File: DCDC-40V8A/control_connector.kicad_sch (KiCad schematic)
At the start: 2 parts, among them J5 Conn_01x08_MountingPin, J6 Conn_01x08_MountingPin

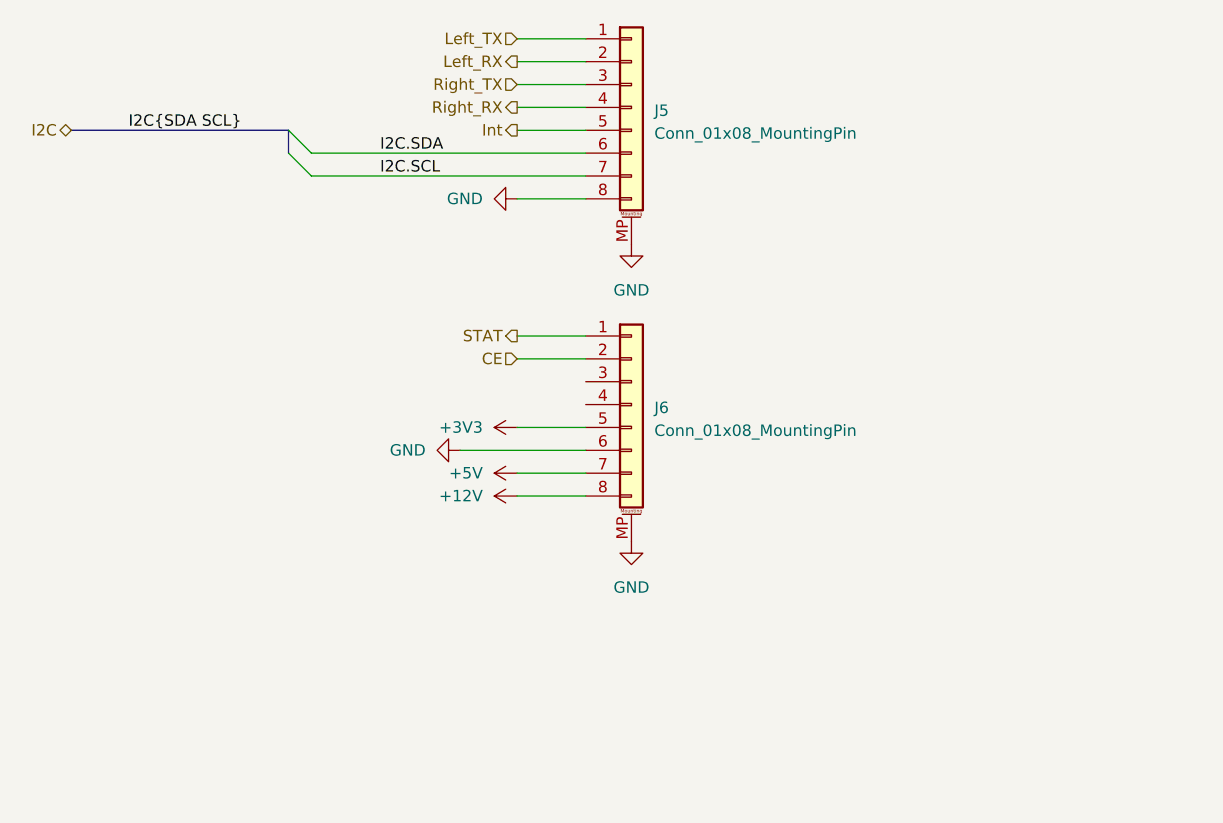
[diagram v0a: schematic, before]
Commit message: some DCDC schematics
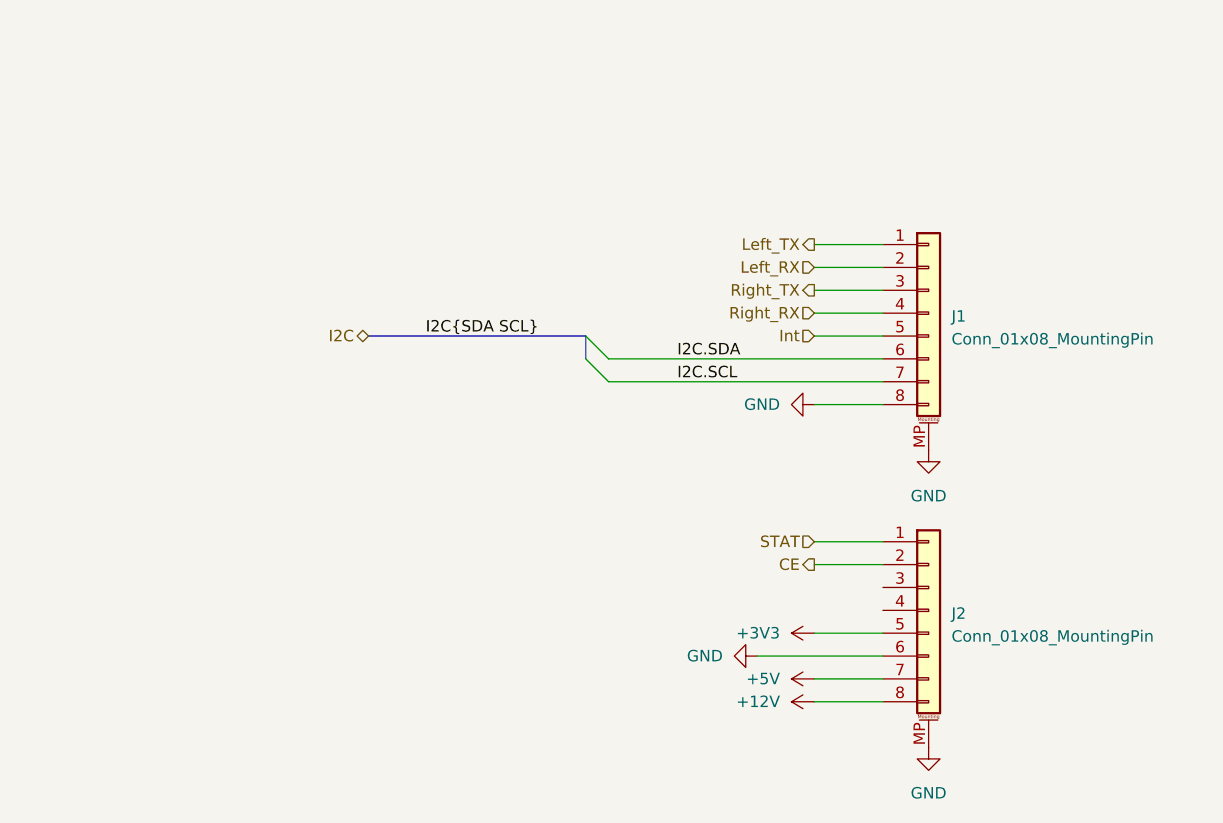
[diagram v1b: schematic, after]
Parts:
- removed J5, J6: Conn_01x08_MountingPin, Connector_JST:JST_SH_SM08B-SRSS-TB_1x08-1MP_P1.00mm_Horizontal, symbol Connector_Generic_MountingPin:Conn_01x08_MountingPin
- added J1, J2: Conn_01x08_MountingPin, Connector_JST:JST_SH_BM08B-SRSS-TB_1x08-1MP_P1.00mm_Vertical, symbol Connector_Generic_MountingPin:Conn_01x08_MountingPin
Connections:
- net +12V: now also J2.8 (Pin_8)
- net +3V3: now also J2.5 (Pin_5)
- net +5V: now also J2.7 (Pin_7)
- net CE: now also J2.2 (Pin_2)
- net GND: now also J1.8 (Pin_8), J1.MP (MountPin), J2.6 (Pin_6), J2.MP (MountPin)
- net I2C.SCL: now also J1.7 (Pin_7)
- net I2C.SDA: now also J1.6 (Pin_6)
- net Int: now also J1.5 (Pin_5)
- net Left_RX: now also J1.2 (Pin_2)
- net Left_TX: now also J1.1 (Pin_1)
- net Right_RX: now also J1.4 (Pin_4)
- net Right_TX: now also J1.3 (Pin_3)
- net STAT: now also J2.1 (Pin_1)

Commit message: wip
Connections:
- net +5V_USB: now reaches J2.3 (Pin_3)
- net +5V_USB: now also J2.4 (Pin_4)
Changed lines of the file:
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@@
 	(generator_version "9.0")
 	(paper "A4")
+	(junction
+		(at 137.16 97.79)
+		(diameter 0)
+		(color 0 0 0 0)
+	)
 	(bus_entry
 		(at 111.76 71.12)
@@
 	(wire
 		(pts
+			(xy 137.16 96.52) (xy 137.16 97.79)
+		)
+		(stroke
+			(width 0)
+			(type default)
+		)
+	)
+	(wire
+		(pts
 			(xy 137.16 63.5) (xy 144.78 63.5)
+		)
+		(stroke
+			(width 0)
+			(type default)
+		)
+	)
+	(wire
+		(pts
+			(xy 144.78 96.52) (xy 137.16 96.52)
+		)
+		(stroke
+			(width 0)
+			(type default)
+		)
+	)
+	(wire
+		(pts
+			(xy 137.16 99.06) (xy 144.78 99.06)
+		)
+		(stroke
+			(width 0)
+			(type default)
+		)
+	)
+	(wire
+		(pts
+			(xy 137.16 97.79) (xy 137.16 99.06)
 		)
 		(stroke
@@
 		)
 	)
+	(symbol
+		(lib_id "power:+5V")
+		(at 137.16 97.79 90)
+		(unit 1)
+		(exclude_from_sim no)
+		(in_bom yes)
+		(on_board yes)
+		(dnp no)
+		(fields_autoplaced yes)
+		(property "Reference" "#PWR054"
+			(at 140.97 97.79 0)
+			(effects
+				(font
+					(size 1.27 1.27)
+				)
+				(hide yes)
+			)
+		)
+		(property "Value" "+5V_USB"
+			(at 133.35 97.7899 90)
+			(effects
+				(font
+					(size 1.27 1.27)
+				)
+				(justify left)
+			)
+		)
+		(property "Footprint" ""
+			(at 137.16 97.79 0)
+			(effects
+				(font
+					(size 1.27 1.27)
+				)
+				(hide yes)
+			)
+		)
+		(property "Datasheet" ""
+			(at 137.16 97.79 0)
+			(effects
+				(font
+					(size 1.27 1.27)
+				)
+				(hide yes)
+			)
+		)
+		(property "Description" "Power symbol creates a global label with name \"+5V\""
+			(at 137.16 97.79 0)
+			(effects
+				(font
+					(size 1.27 1.27)
+				)
+				(hide yes)
+			)
+		)
+		(pin "1"
+		)
+		(instances
+			(project ""
+				(path "/c2f330be-6ca8-4ed0-86db-c2e1bfb68425/54fe40ea-071e-47fc-93b0-08edbf0643ce"
+					(reference "#PWR054")
+					(unit 1)
+				)
+			)
+		)
+	)

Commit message: renumbering
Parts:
- renumbered J1 to J3, J2 to J4
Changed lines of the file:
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@@
 		(dnp no)
 		(fields_autoplaced yes)
-		(property "Reference" "#PWR054"
+		(property "Reference" "#PWR045"
 			(at 140.97 97.79 0)
 			(hide yes)
@@
 			(project "DCDC-40V8A"
 				(path "/c2f330be-6ca8-4ed0-86db-c2e1bfb68425/54fe40ea-071e-47fc-93b0-08edbf0643ce"
-					(reference "#PWR054")
+					(reference "#PWR045")
 					(unit 1)
 				)
@@
 		(dnp no)
 		(fields_autoplaced yes)
-		(property "Reference" "#PWR02"
+		(property "Reference" "#PWR050"
 			(at 149.86 120.65 0)
 			(hide yes)
@@
 			(project "DCDC-40V8A"
 				(path "/c2f330be-6ca8-4ed0-86db-c2e1bfb68425/54fe40ea-071e-47fc-93b0-08edbf0643ce"
-					(reference "#PWR02")
+					(reference "#PWR050")
 					(unit 1)
 				)
@@
 		(dnp no)
 		(fields_autoplaced yes)
-		(property "Reference" "#PWR01"
+		(property "Reference" "#PWR044"
 			(at 149.86 87.63 0)
 			(hide yes)
@@
 			(project "DCDC-40V8A"
 				(path "/c2f330be-6ca8-4ed0-86db-c2e1bfb68425/54fe40ea-071e-47fc-93b0-08edbf0643ce"
-					(reference "#PWR01")
+					(reference "#PWR044")
 					(unit 1)
 				)
@@
 		(dnp no)
 		(fields_autoplaced yes)
-		(property "Reference" "#PWR039"
+		(property "Reference" "#PWR046"
 			(at 140.97 101.6 0)
 			(hide yes)
@@
 			(project "DCDC-40V8A"
 				(path "/c2f330be-6ca8-4ed0-86db-c2e1bfb68425/54fe40ea-071e-47fc-93b0-08edbf0643ce"
-					(reference "#PWR039")
+					(reference "#PWR046")
 					(unit 1)
 				)
@@
 		(dnp no)
 		(fields_autoplaced yes)
-		(property "Reference" "#PWR037"
+		(property "Reference" "#PWR049"
 			(at 140.97 109.22 0)
 			(hide yes)
@@
 			(project "DCDC-40V8A"
 				(path "/c2f330be-6ca8-4ed0-86db-c2e1bfb68425/54fe40ea-071e-47fc-93b0-08edbf0643ce"
-					(reference "#PWR037")
+					(reference "#PWR049")
 					(unit 1)
 				)
@@
 		(dnp no)
 		(fields_autoplaced yes)
-		(property "Reference" "J2"
+		(property "Reference" "J4"
 			(at 152.4 99.4155 0)
 			(show_name no)
@@
 			(project "DCDC-40V8A"
 				(path "/c2f330be-6ca8-4ed0-86db-c2e1bfb68425/54fe40ea-071e-47fc-93b0-08edbf0643ce"
-					(reference "J2")
+					(reference "J4")
 					(unit 1)
 				)
@@
 		(in_pos_files yes)
 		(dnp no)
-		(property "Reference" "#PWR038"
+		(property "Reference" "#PWR048"
 			(at 140.97 106.68 0)
 			(hide yes)
@@
 			(project "DCDC-40V8A"
 				(path "/c2f330be-6ca8-4ed0-86db-c2e1bfb68425/54fe40ea-071e-47fc-93b0-08edbf0643ce"
-					(reference "#PWR038")
+					(reference "#PWR048")
 					(unit 1)
 				)
@@
 		(dnp no)
 		(fields_autoplaced yes)
-		(property "Reference" "#PWR036"
+		(property "Reference" "#PWR043"
 			(at 130.81 76.2 0)
 			(hide yes)
@@
 			(project "DCDC-40V8A"
 				(path "/c2f330be-6ca8-4ed0-86db-c2e1bfb68425/54fe40ea-071e-47fc-93b0-08edbf0643ce"
-					(reference "#PWR036")
+					(reference "#PWR043")
 					(unit 1)
 				)
@@
 		(dnp no)
 		(fields_autoplaced yes)
-		(property "Reference" "#PWR040"
+		(property "Reference" "#PWR047"
 			(at 124.46 104.14 0)
 			(hide yes)
@@
 			(project "DCDC-40V8A"
 				(path "/c2f330be-6ca8-4ed0-86db-c2e1bfb68425/54fe40ea-071e-47fc-93b0-08edbf0643ce"
-					(reference "#PWR040")
+					(reference "#PWR047")
 					(unit 1)
 				)
@@
 		(dnp no)
 		(fields_autoplaced yes)
-		(property "Reference" "J1"
+		(property "Reference" "J3"
 			(at 152.4 66.3955 0)
 			(show_name no)
@@
 			(project "DCDC-40V8A"
 				(path "/c2f330be-6ca8-4ed0-86db-c2e1bfb68425/54fe40ea-071e-47fc-93b0-08edbf0643ce"
-					(reference "J1")
-					(unit 1)
-				)
+					(reference "J3")
+					(unit 1)
+				)
